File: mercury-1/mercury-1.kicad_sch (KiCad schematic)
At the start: 76 parts, among them J1 +22.2V Logic Battery Array, J10 Andersen Connector, J11 Andersen Connector, J12 Andersen Connector, J13 Andersen Connector, J14 DB25 Encoder Harness, J15 P-20-90-PRO-121-B, J16 RJ-45 Bulkhead, J17 USB_Bulkhead, J2 +14.4V Drivetrain Battery Arr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, J3 +22.2V A/S Battery Array, J4 Jetson, J5 POE Injector, J6 Network Switch, J7 P-17-80-PRO-121-B, J8 Andersen Connector, J9 Andersen Connector, K1 200A Relay 12V Coil, K2 200A Relay 12V Coil, K3 200A Relay 12V Coil, K4 200A Relay 12V Coil, K5 200A Relay 12V Coil, K6 200A Relay 12V Coil, K7 200A Relay 12V Coil, K8 200A Relay 12V Coil, M1 Yellowjacket 5203, M10 NEO_Brushless_Motor, M2 FGA-32124500-G1166, M3 FGA-32124500-G1166, M4 Yellowjacket 5203, M5 NEO_Brushless_Motor, M6 NEO_Brushless_Motor, M7 NEO_Brushless_Motor, M8 NEO_Brushless_Motor, M9 NEO_Brushless_Motor, SW1 SW_SPDT_321, U1 UVLO Relay, U10 MAX6675 Breakout, U11 MAX6675 Breakout, U12 MAX6675 Breakout, U13 MAX6675 Breakout, U14 MAX6675 Breakout, U15 RoboClaw_2x7A, U16 RoboClaw_2x7A, U17 5k (8mm Bore), U18 ODESC_V4.2, U19 ODESC_V4.2, U2 Buck Converter, U20 ODESC_V4.2, U21 ODESC_V4.2, U22 ODESC_V4.2, U23 ODESC_V4.2, U24 5k (8mm Bore), U3 Buck Converter, U4 UVLO Relay, U5 Logic Relay, U6 Logic Relay, U7 UVLO Relay, U8 RASPBERRY_PI_4B_4GB, U9 MAX6675 Breakout

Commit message: off
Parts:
- removed M2, M3: FGA-32124500-G1166, symbol logic_board:FGA-32124500-G1166
- removed R7, R8: 7.5k, symbol Device:R_US
- removed U17, U24: 5k (8mm Bore), symbol logic_board:NP32HS
- added M2, M3: Yellowjacket 5203, symbol logic_board:Yellowjacket 5203
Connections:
- net Axis_4+: now also M2.1 (+)
- net Axis_4-: now also M2.2 (-)
- net Axis_5+: now also M3.1 (+)
- net Axis_5-: now also M3.2 (-)
- net CAN_H_ARM: now also J14.4, J14.5; no longer J14.21 (P21), J14.9
- net EF_5V: now also J14.8; no longer J14.23 (P23)
- net EF_CHA: now also J14.7; no longer J14.22 (P22)
- net EF_CHB: now also J14.6; no longer J14.10
- net EF_GND: now also J14.9; no longer J14.11
- net axis1_5V: now also J14.12; no longer J14.25 (P25)
- net axis1_CHA: now also J14.11; no longer J14.24 (P24)
- net axis1_CHB: now also J14.10; no longer J14.12
- net axis4_AO: no longer J14.20 (P20)
- net axis4_E_GND: no longer J14.7
- net axis4_PU: no longer J14.8
- net axis5_AO: no longer J14.6
- net axis5_E_GND: no longer J14.18 (P18)
- net axis5_PU: no longer J14.19 (P19)
- new net axis4_5V: J14.24 (P24)
- new net axis4_CHA: J14.23 (P23)
- new net axis4_CHB: J14.22 (P22)
- new net axis4_GND: J14.25 (P25)
- new net axis5_5V: J14.20 (P20)
- new net axis5_CHA: J14.19 (P19)
- new net axis5_CHB: J14.18 (P18)
- new net axis5_GND: J14.21 (P21)
- no-connect marks 149 -> 147
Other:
- note removed: "Analog Encoders for Axis 4,5"
- moved on the sheet: J14, R9

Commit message: Changed pinouts
Fixed Serial for Roboclaws. Changed power sequencing to jetson
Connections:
- net +22.2V_A/S_OUT: no longer U15.36 (M_GND)
- net GPIO17: no longer U15.7 (S2)
- net GPIO35: now also U6.6 (EN); no longer U16.7 (S2)
- net GPIO8: now also U5.6 (EN); no longer U15.3 (S1), U16.3 (S1)
- net UART1_RX: now reaches J4.10 (Pin_10)
- net UART1_RX: now also U15.7 (S2), U16.7 (S2)
- net UART1_TX: now reaches J4.8 (Pin_8)
- net UART1_TX: now also U15.3 (S1), U16.3 (S1)
- net PI_GPIO5: no longer names the net of U8.29 (GPIO5)
- net PI_GPIO5: no longer U5.6 (EN)
- net PI_GPIO6: no longer names the net of U8.31 (GPIO6)
- net PI_GPIO6: no longer U6.6 (EN)
- no-connect marks 147 -> 145
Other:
- moved on the sheet: U15

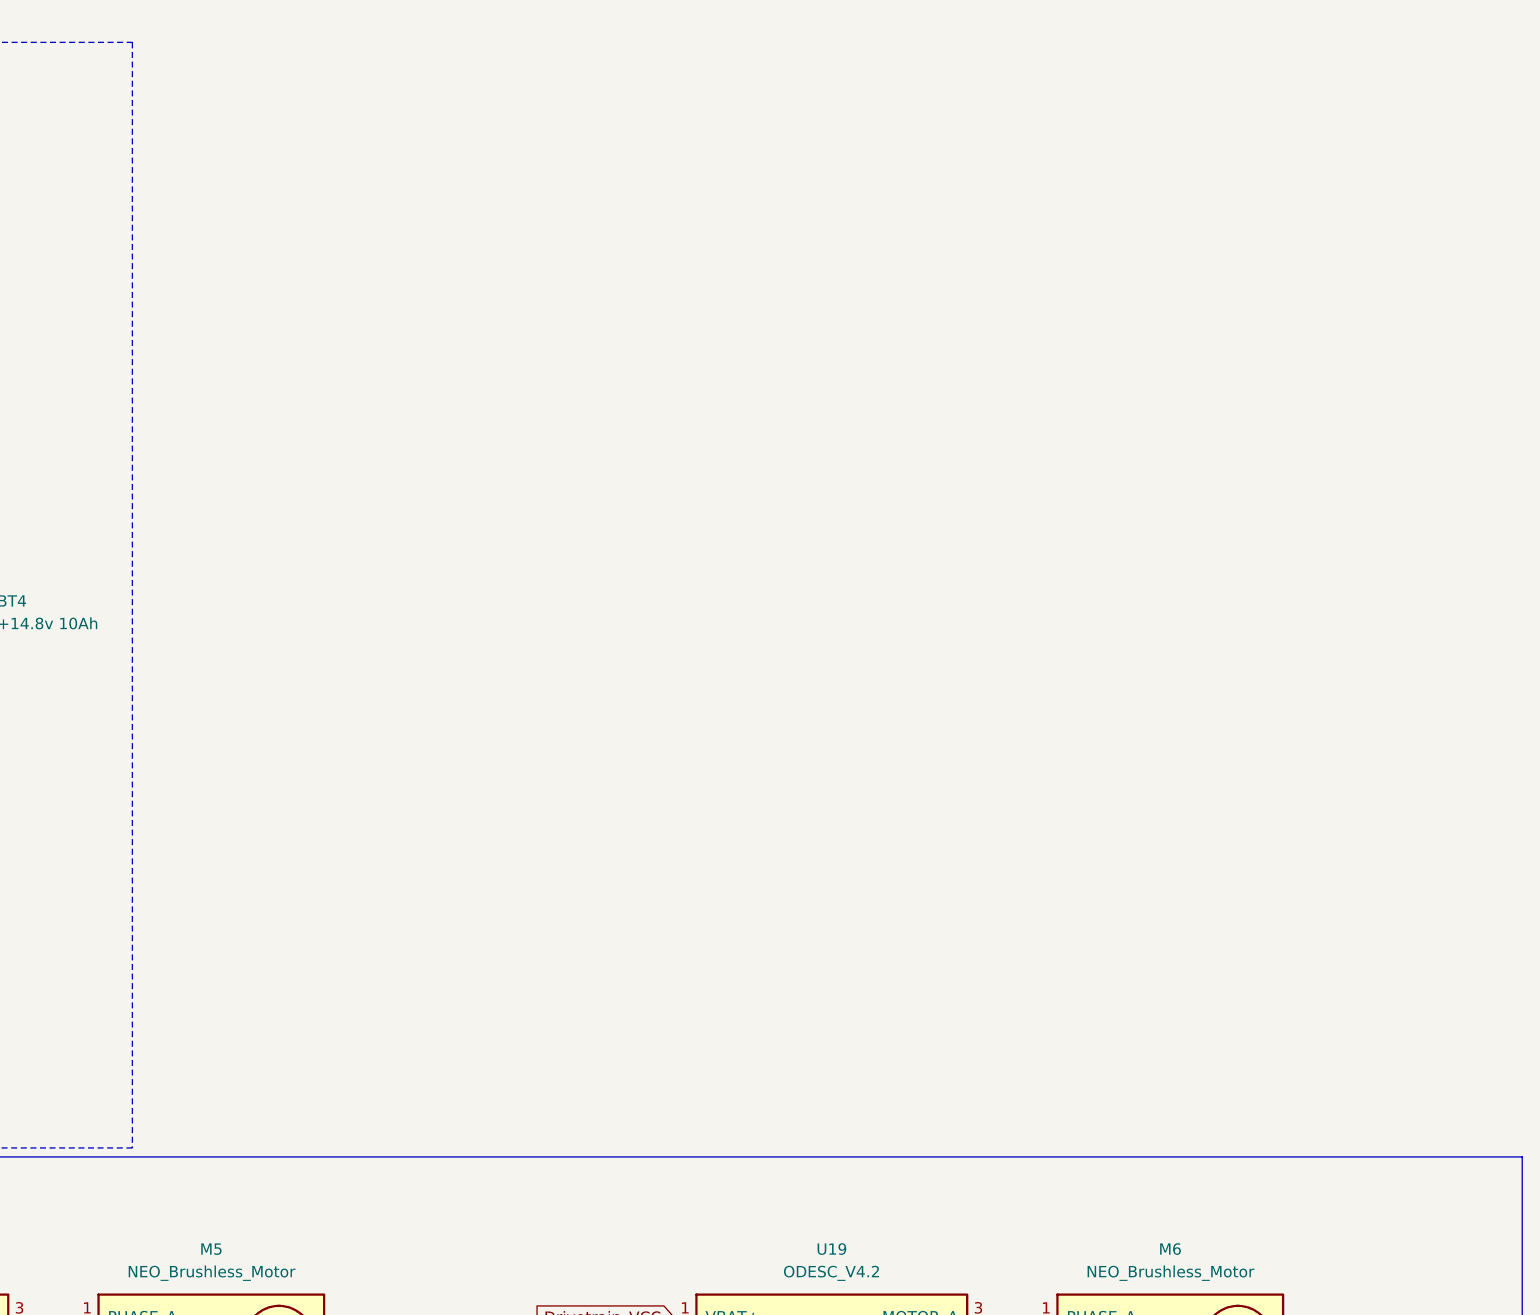
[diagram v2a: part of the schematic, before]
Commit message: Added Science Subsystem to Schematic
Updated code to correct Hbridge issues as well.
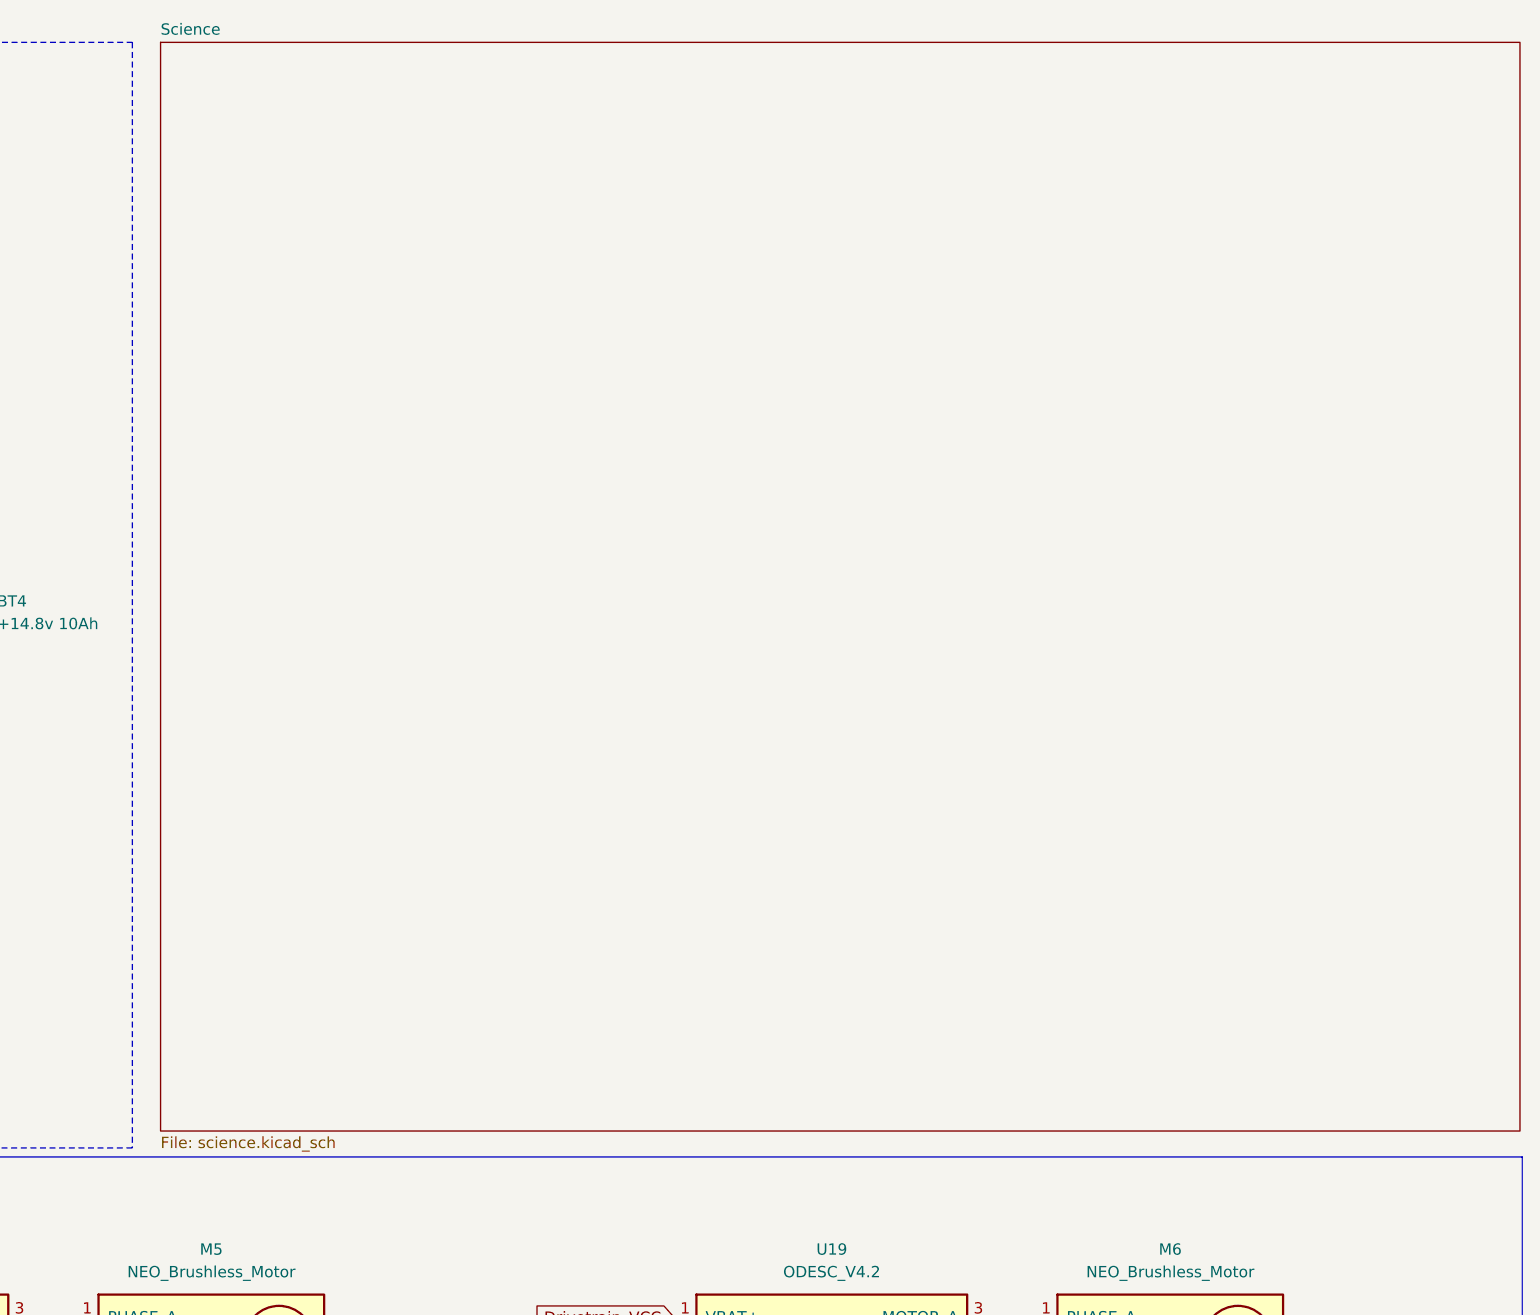
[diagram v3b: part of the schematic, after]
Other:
- added sheet Science (science.kicad_sch)
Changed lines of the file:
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@@
+		)
+	)
+	(sheet
+		(at 428.625 13.97)
+		(size 153.035 122.555)
+		(exclude_from_sim no)
+		(in_bom yes)
+		(on_board yes)
+		(dnp no)
+		(fields_autoplaced yes)
+		(stroke
+			(width 0.1524)
+			(type solid)
+		)
+		(fill
+			(color 0 0 0 0.0000)
+		)
+		(property "Sheetname" "Science"
+			(at 428.625 13.2584 0)
+			(effects
+				(font
+					(size 1.27 1.27)
+				)
+				(justify left bottom)
+			)
+		)
+		(property "Sheetfile" "science.kicad_sch"
+			(at 428.625 137.1096 0)
+			(effects
+				(font
+					(size 1.27 1.27)
+				)
+				(justify left top)
+			)
+		)
+		(instances
+			(project "mercury-1"
+				(path "/1b548578-061f-412b-9a17-10125f836cd9"
+					(page "2")
+				)
+			)
 		)
 	)
